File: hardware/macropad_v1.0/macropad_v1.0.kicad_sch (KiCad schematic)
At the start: 44 parts, among them J1 USB_C_Receptacle_USB2.0_14P, SW1 SW_Push, SW2 Rotary Encoder, U1 USBLC6-2SC6, U2 STM32F072C8T6, U3 XC6206PxxxMR

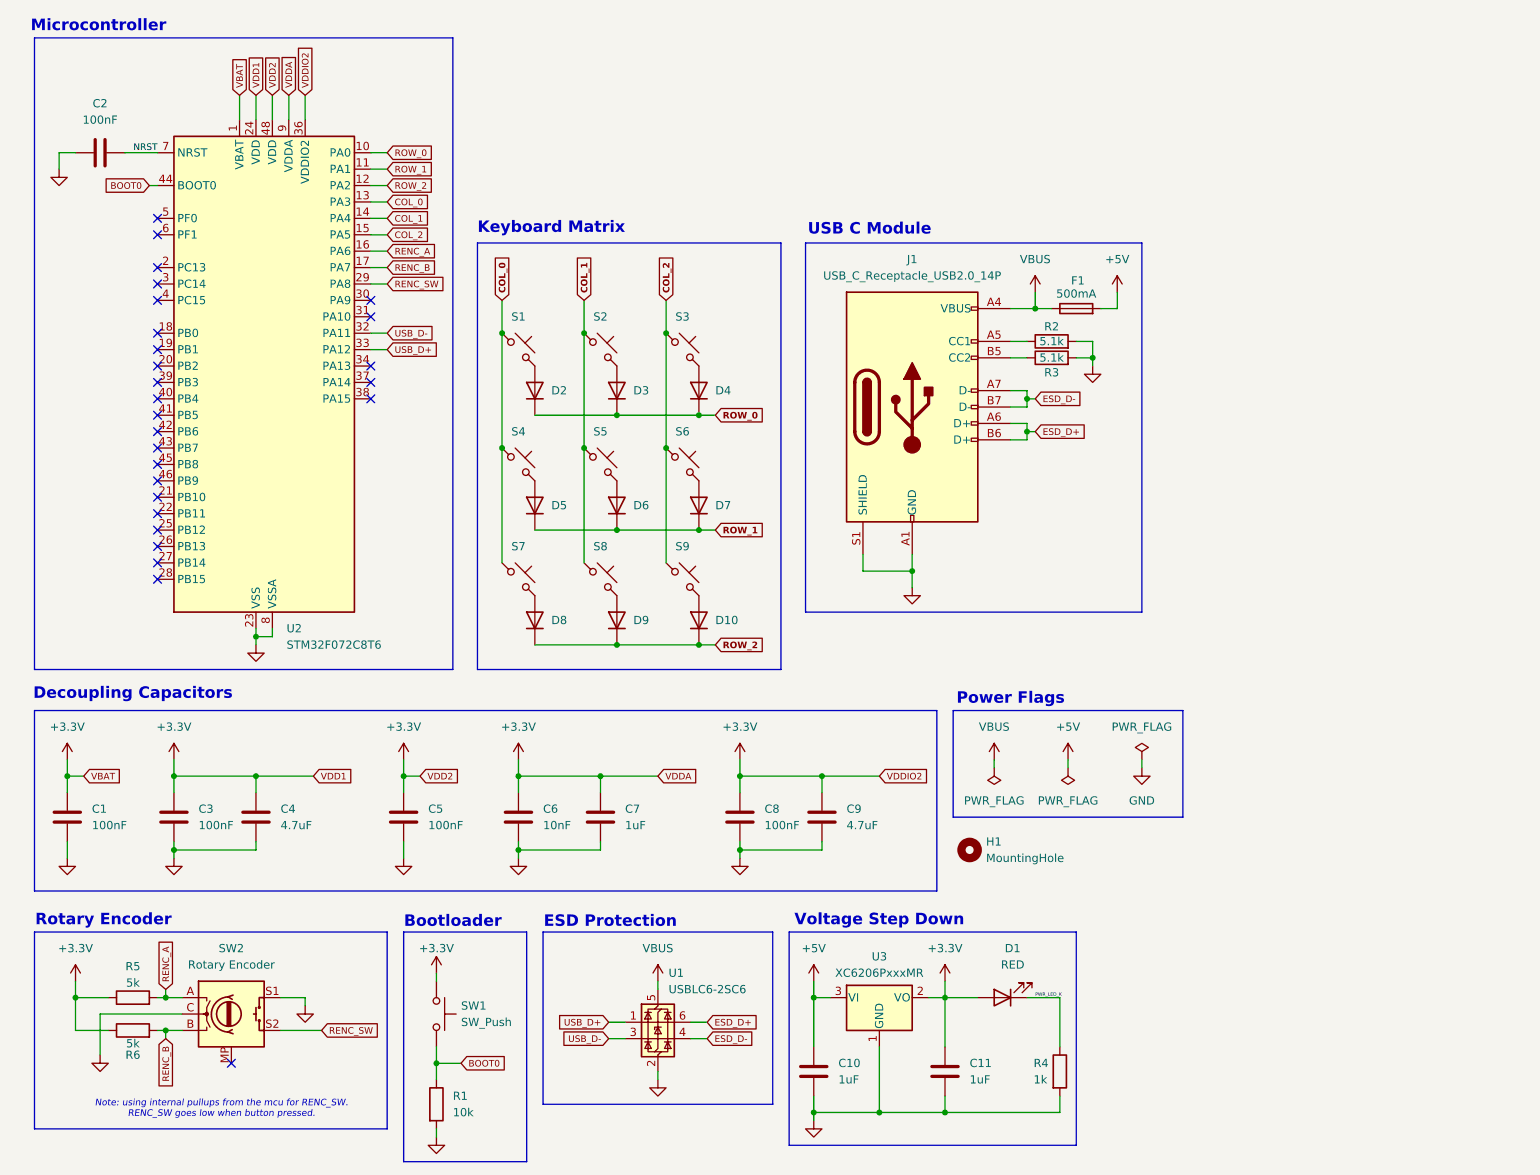
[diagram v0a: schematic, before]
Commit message: added second rotary encoder, made progress on layout
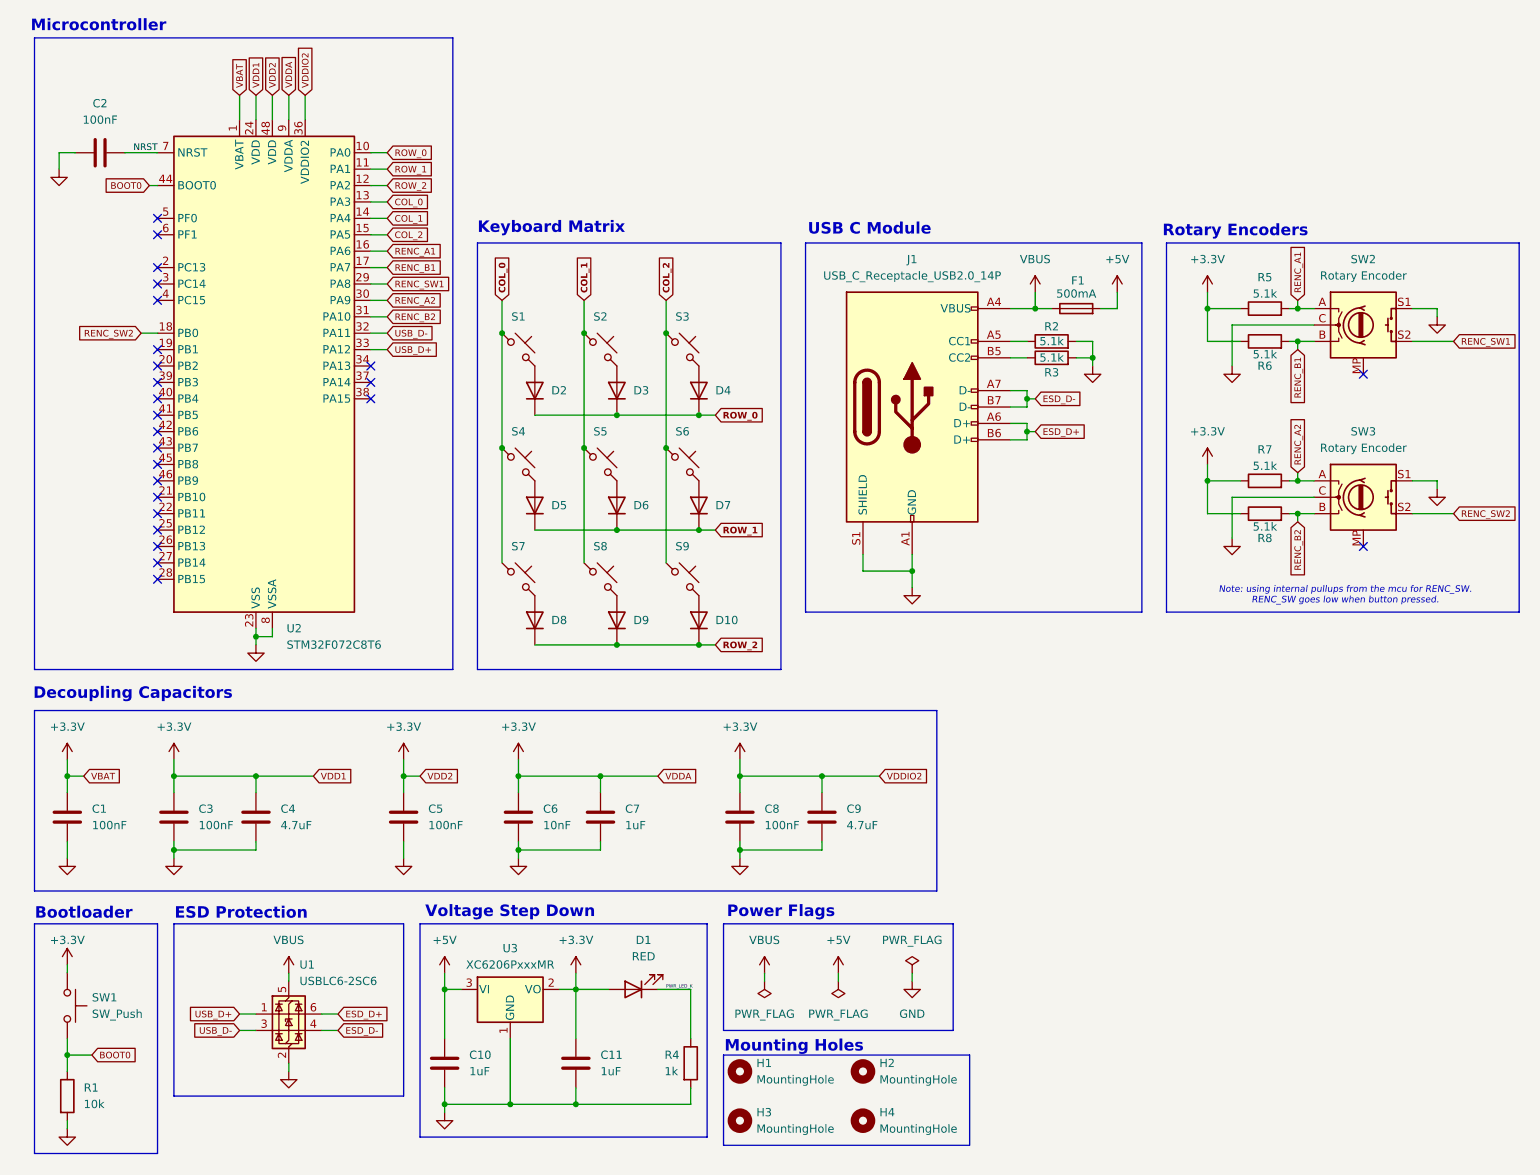
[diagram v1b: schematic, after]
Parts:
- added H2, H3, H4: MountingHole, MountingHole:MountingHole_2.2mm_M2, symbol Mechanical:MountingHole
- added R7, R8: 5.1k, Resistor_SMD:R_0603_1608Metric_Pad0.98x0.95mm_HandSolder, symbol Device:R
- added SW3: Rotary Encoder, Rotary_Encoder:RotaryEncoder_Alps_EC11E-Switch_Vertical_H20mm, symbol Device:RotaryEncoder_Switch_MP
- C1, C10, C11, C2, C3, C4, C5, C6, C7, C8, C9: footprint (none) -> Capacitor_SMD:C_0603_1608Metric_Pad1.08x0.95mm_HandSolder
- D1: footprint (none) -> LED_SMD:LED_0603_1608Metric_Pad1.05x0.95mm_HandSolder
- D10, D2, D3, D4, D5, D6, D7, D8, D9: footprint (none) -> Diode_SMD:D_SOD-123
- F1: footprint (none) -> Fuse:Fuse_1206_3216Metric_Pad1.42x1.75mm_HandSolder
- H1: footprint (none) -> MountingHole:MountingHole_2.2mm_M2
- J1: footprint (none) -> Connector_USB:USB_C_Receptacle_HRO_TYPE-C-31-M-12
- R1, R2, R3, R4: footprint (none) -> Resistor_SMD:R_0603_1608Metric_Pad0.98x0.95mm_HandSolder
- R5, R6: value 5k -> 5.1k; footprint (none) -> Resistor_SMD:R_0603_1608Metric_Pad0.98x0.95mm_HandSolder
- S1, S2, S3, S4, S5, S6, S7, S8, S9: footprint (none) -> ScottoKeebs_MX:MX_PCB_1.00u
- SW1: footprint (none) -> Button_Switch_SMD:SW_SPST_EVQP7C
- SW2: footprint (none) -> Rotary_Encoder:RotaryEncoder_Alps_EC11E-Switch_Vertical_H20mm
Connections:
- net +3.3V: now also R7.1, R8.1
- net GND: now also SW3.C, SW3.S1
- net RENC_SW2: now reaches U2.18 (PB0)
- net RENC_SW2: now also SW3.S2
- net RENC_A2: now reaches U2.30 (PA9)
- net RENC_A2: now also R7.2, SW3.A
- net RENC_B2: now reaches U2.31 (PA10)
- net RENC_B2: now also R8.2, SW3.B
- net RENC_A renamed RENC_A1
- net RENC_B renamed RENC_B1
- net RENC_SW renamed RENC_SW1
- no-connect marks 27 -> 25
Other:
- note added: "Mounting Holes"
- note added: "Rotary Encoders"
- note removed: "Rotary Encoder"
- moved on the sheet: C10, C11, D1, H1, R1, R4, R5, R6, SW1, SW2, U1, U3

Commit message: updated some 3d models, finished routing usb and esd protection
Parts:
- SW1: footprint Button_Switch_SMD:SW_SPST_EVQP7C -> ScottoKeebs_Components:Button_TL3342
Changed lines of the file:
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@@
 			)
 		)
-		(property "Footprint" "Button_Switch_SMD:SW_SPST_EVQP7C"
+		(property "Footprint" "ScottoKeebs_Components:Button_TL3342"
 			(at 24.13 172.72 0)
 			(effects

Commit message: forgot to save schematic
-exact changes can be found in old commit, I think it was just changing the name in the title block to say ParPad
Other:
- title: Macropad -> ParPad v1.0
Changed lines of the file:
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@@
 	(paper "A4")
 	(title_block
-		(title "Macropad")
+		(title "ParPad v1.0")
 		(date "2025-05-25")
 		(rev "v1.0")
